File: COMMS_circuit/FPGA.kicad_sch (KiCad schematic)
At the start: 29 parts, among them U15 ICE40HX4K-TQ144

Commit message: Changes I missed cause id been staring at it to long
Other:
- moved on the sheet: C56, C57, C58, C59, C64, C65, C66, C67, C68, C69, C70, C71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

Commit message: testing opsec update
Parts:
- added J5: Conn_01x12_Pin, Connector_PinHeader_2.54mm:PinHeader_1x12_P2.54mm_Vertical, symbol Connector:Conn_01x12_Pin
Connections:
- net +3V3: now also J5.11 (Pin_11)
- net DGND: now also J5.1 (Pin_1)
- net TTCK: now also U15.1 (IOL_2A)
- net at U15.10 (IOL_5B): now also J5.5 (Pin_5)
- net at U15.11 (IOL_8A): now also J5.6 (Pin_6)
- net at U15.12 (IOL_8B): now also J5.7 (Pin_7)
- net at U15.15 (IOL_10A): now also J5.8 (Pin_8)
- net at U15.16 (IOL_10B): now also J5.9 (Pin_9)
- net at U15.17 (IOL_12A): now also J5.10 (Pin_10)
- net at U15.7 (IOL_4A): now also J5.2 (Pin_2)
- net at U15.8 (IOL_4B): now also J5.3 (Pin_3)
- net at U15.9 (IOL_5A): now also J5.4 (Pin_4)
- new net +5V: J5.12 (Pin_12)
- no-connect marks 1 -> 60
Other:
- moved on the sheet: C59, U15D

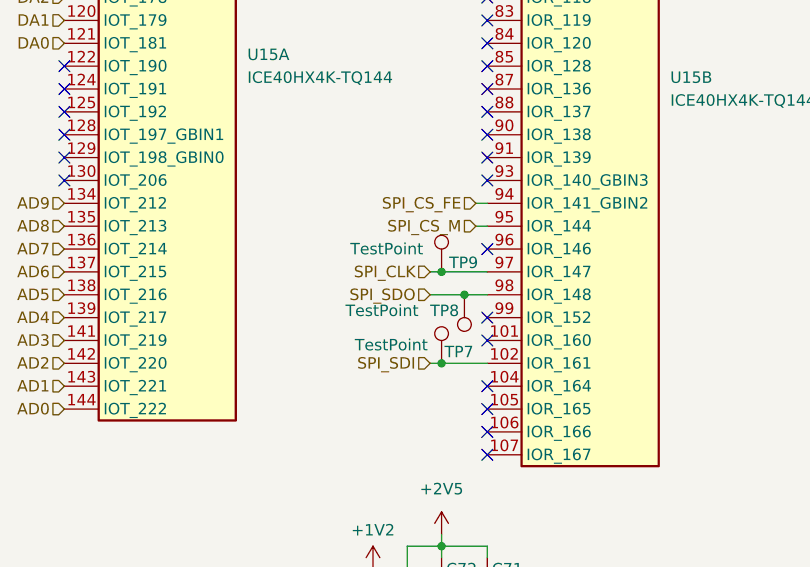
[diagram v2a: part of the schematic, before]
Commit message: Stick a RP2040 on the side and see if we can program an FPGA with it
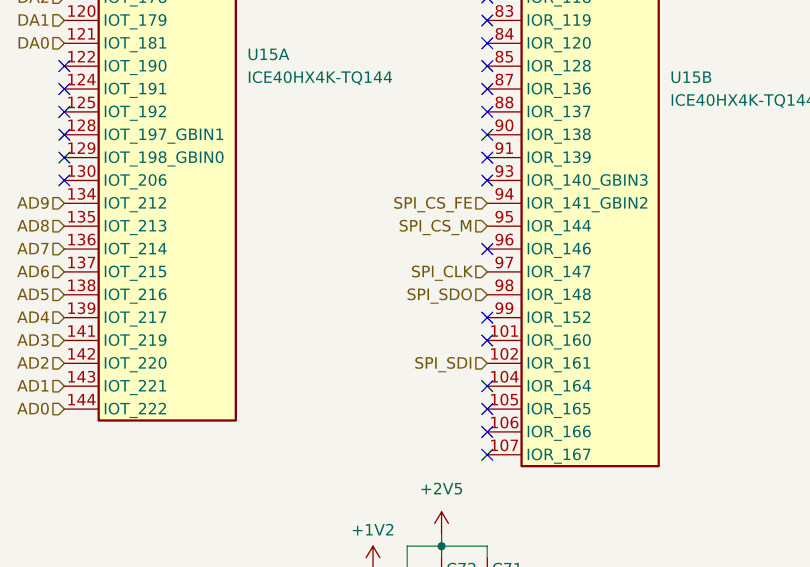
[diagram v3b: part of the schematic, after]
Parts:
- removed TP7, TP8, TP9: TestPoint, TestPoint:TestPoint_Keystone_5000-5004_Miniature, symbol Connector:TestPoint
